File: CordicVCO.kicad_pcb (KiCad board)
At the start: 2 copper layers, 50.8 x 27.9 mm, 1 part, among them U1 STM32G431

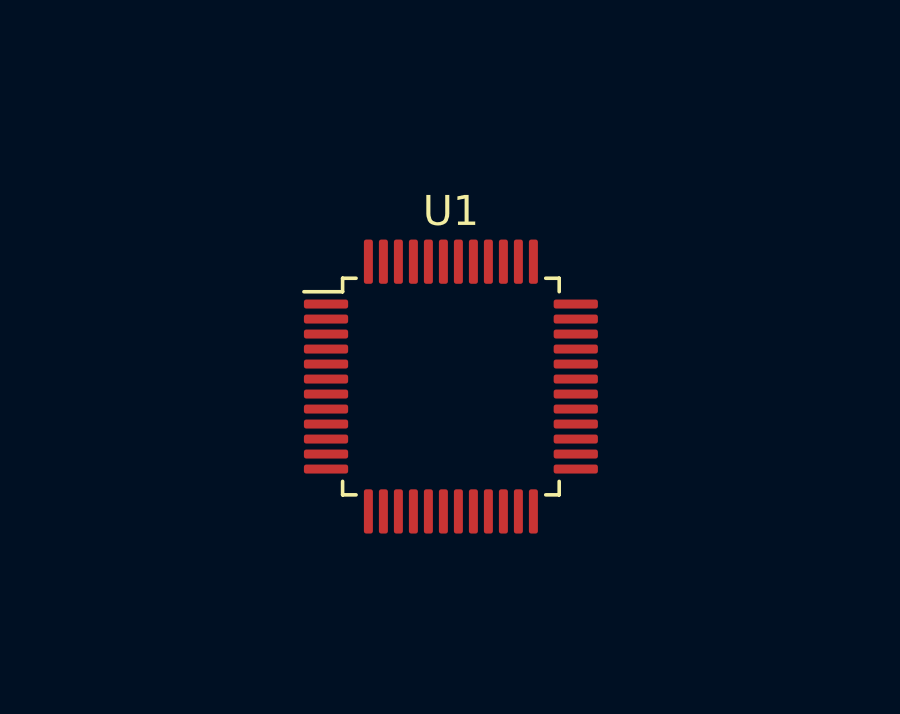
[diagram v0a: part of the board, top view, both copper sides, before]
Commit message: Major pin-assignments and some IO hardware.
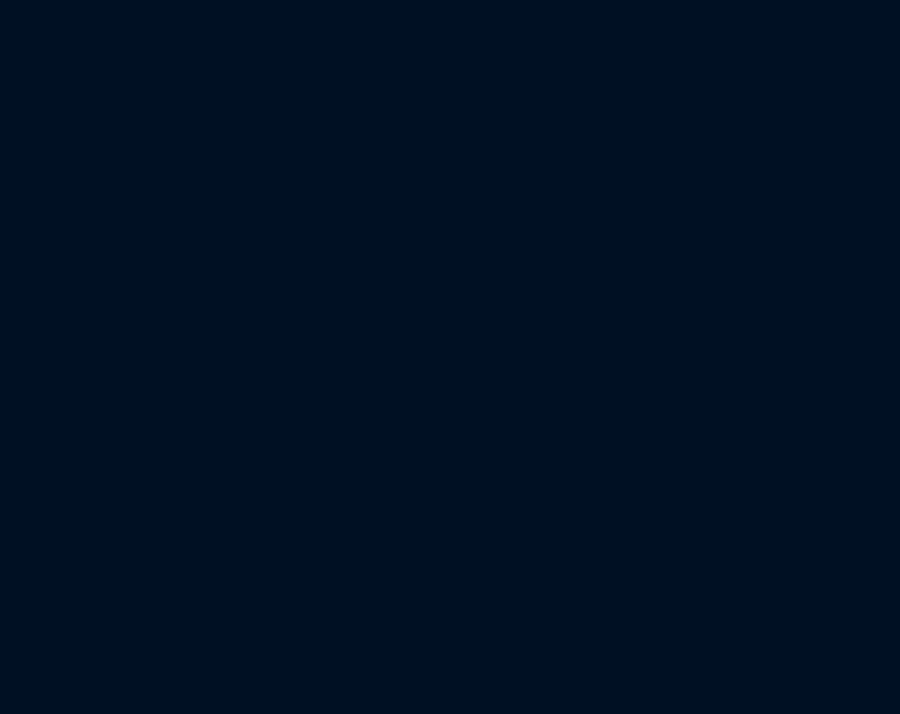
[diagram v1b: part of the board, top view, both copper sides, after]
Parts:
- removed U1: STM32G431, Package_QFP:LQFP-48_7x7mm_P0.5mm
